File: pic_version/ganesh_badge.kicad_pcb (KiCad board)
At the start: 2 copper layers, 36 x 47.8 mm, 14 parts, among them J1 Conn_01x03_Male, J2 USB_B_Micro, SW1 SW_Push, U1 PIC10F202T-I/OT

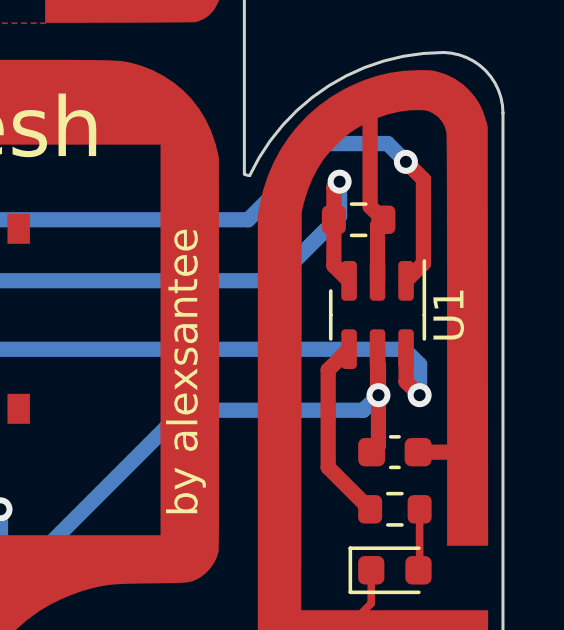
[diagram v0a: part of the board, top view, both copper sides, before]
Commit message: simple text fixes
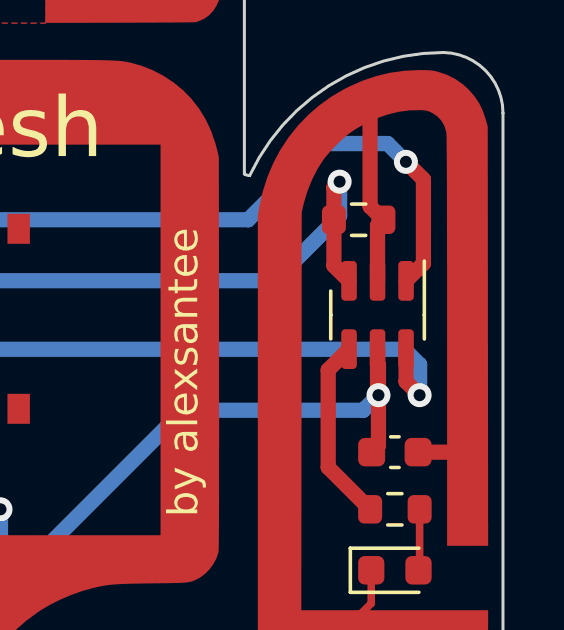
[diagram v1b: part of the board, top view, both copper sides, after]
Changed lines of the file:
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@@
     (property "Sheetname" "")
     (attr smd)
-    (fp_text reference "U1" (at 0 -2.4 -90) (layer "F.SilkS")
+    (fp_text reference "U1" (at 0 -2.4 -90) (layer "F.SilkS") hide
       (effects (font (size 1 1) (thickness 0.15)))
     )
